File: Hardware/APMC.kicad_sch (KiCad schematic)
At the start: 180 parts, among them J1 Pin header Male 2x7 P:1.27, J10 Conn_01x03, J11 Conn_01x03, J12 Conn_01x08, J13 Conn_01x03, J14 Conn_01x04, J15 Pins 1x08, J2 USB4105-GF-A, J5 Terminal 1x5 P:3.5mm, J6 Terminal 1x5 P:3.5mm, J7 Terminal 1x5 P:3.5mm, J8 Conn_01x04, J9 Conn_01x04, M1 Logo_Open_Hardware_Small, Q1 FDT86102LZ, Q2 DMP6023LE, Q3 DMP6023LE, Q4 BSS123, Q5 DMP6023LE, Q6 DMP6023LE, Q7 BSS123, U10 TXU0202, U11 PCA9306, U12 LM74703/LM74704, U13 TPS62162DSG, U14 OPA2387DSG, U15 TPS259461A, U16 TUSB320, U17 LMR38015, U2 LCFE201202A, U3 TXU0202, U4 M95P32, U5 STM32U575CITx, U6 XTR200, U7 TPS7A2031PDBVR, U8 XTR200, U9 ADS1x2S14, X1 SiT8008Bx-7x, Y1 32.768kHz

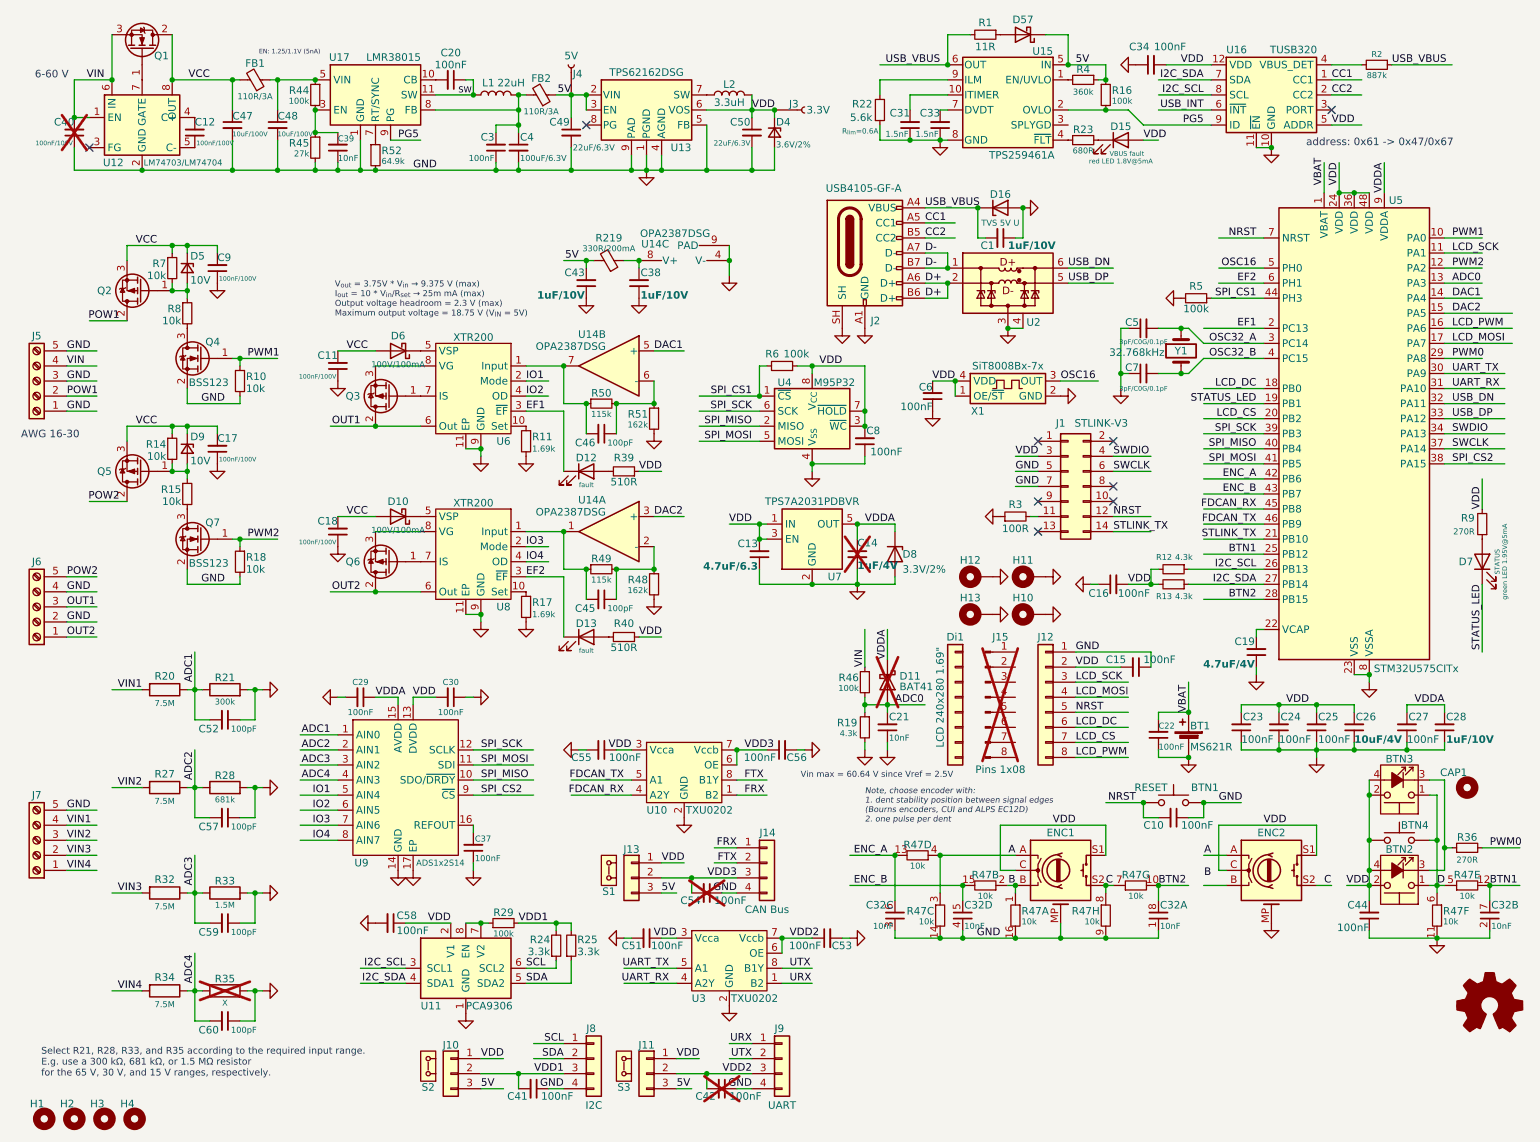
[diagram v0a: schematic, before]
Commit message: work on ADC communication
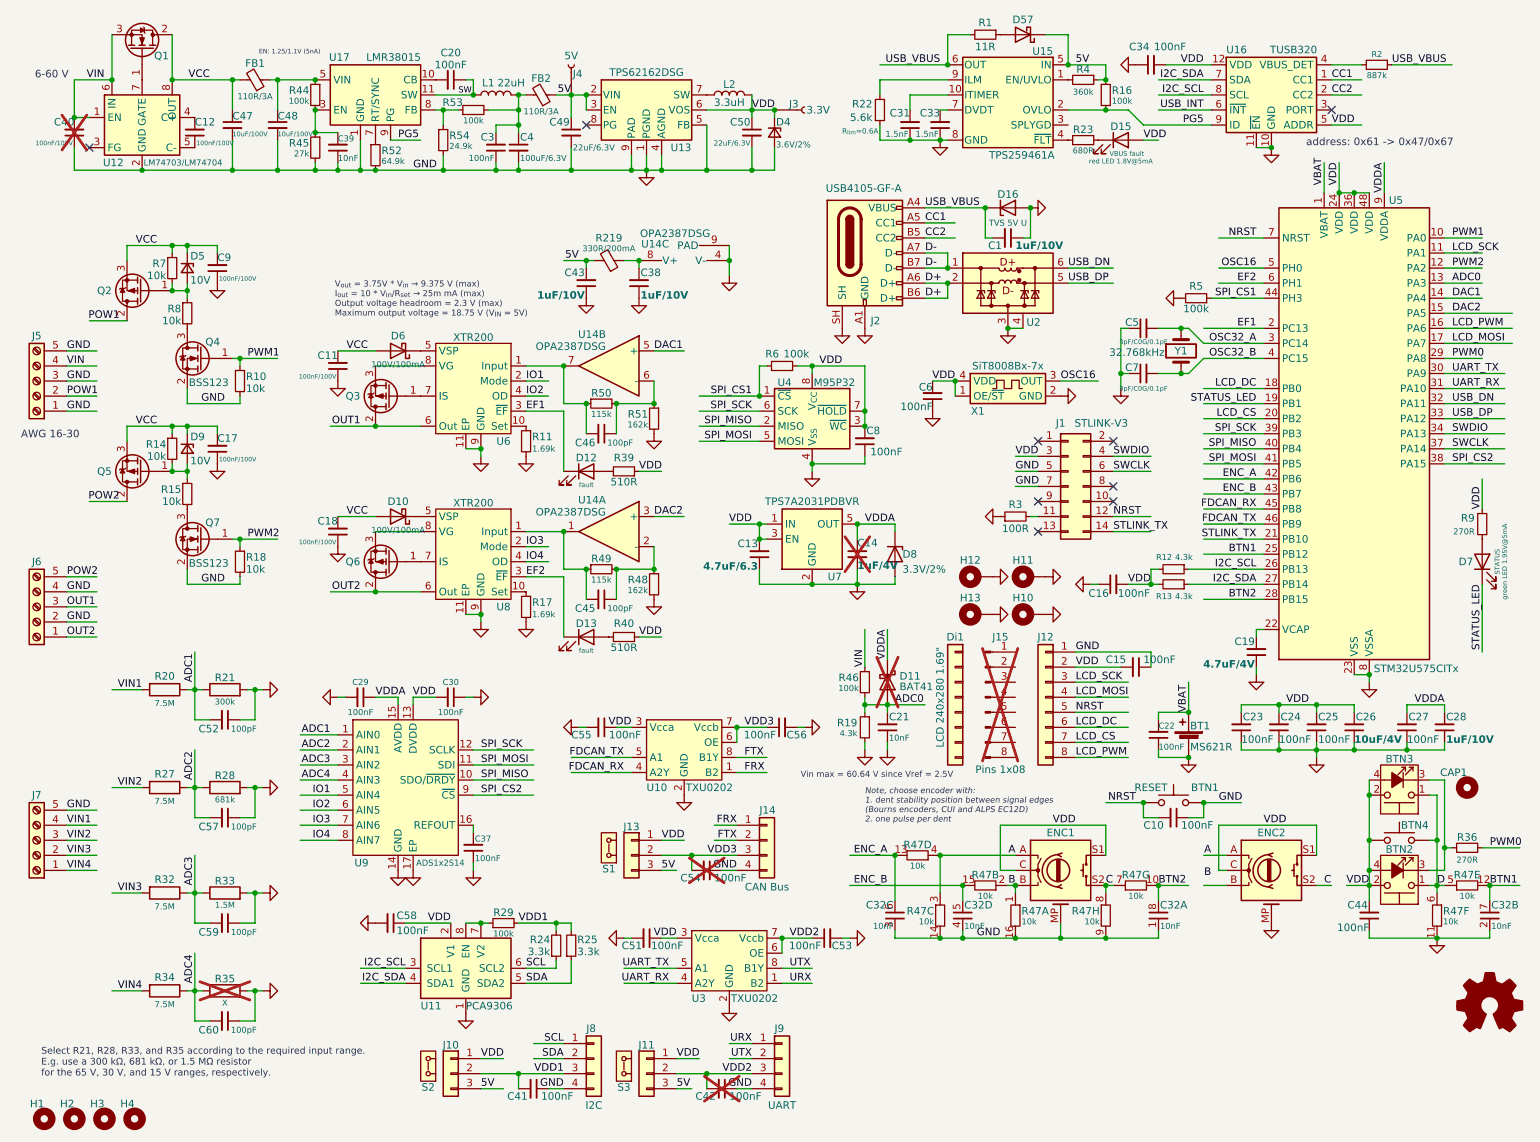
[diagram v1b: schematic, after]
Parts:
- added R53: 100k, Resistor_SMD:R_0603_1608Metric_Pad0.98x0.95mm_HandSolder, symbol Device:R_Small
- added R54: 24.9k, Resistor_SMD:R_0603_1608Metric_Pad0.98x0.95mm_HandSolder, symbol Device:R_Small
- BTN3: footprint tactile_switch_6x6_LED -> Custom:tactile_switch_6x6_LED
- D16: footprint Custom:D_SOD-123F -> Custom:D_SOD-123FL2; Alt many, eg. Littelfuse: SZSMF6L5.0AT3G, TSMC: SMF4L5.0A -> SMF4L5.0A, TPSMF4L5.0A, SMF4L5.0AT1G, PTVS5V0S1UTR,115; Mfg Littelfuse: SZSMF6L5.0AT3G -> Littelfuse: SMF4L5.0A; Mouser 576-SZSMF6L5.0AT3G -> 576-SMF4L5.0A
- L1: 10x10 DD1274AS-H-330M=P3, MSS1048-333MLC, CDRH104NP-330MC, 744771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 -> 1274AS-H-220M=P3, DD1274AS-H-220M=P3, MBH10145C-220MA=P3, B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; 8x8 (none) -> 1273AS-H-220M=P3, 1217AS-H-220M=P3; Ferrite 8x8 CDRH8D28NP-330NC, CDRH8D28NP-330NC, CDRH8D43HPNP-330NC, SCR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 -> (none); Mfg Murata: 1248AS-H-330M=P3 -> Murata: 1274AS-H-220M=P3; Mouser 81-1248AS-H-330MP3 -> 81-1274AS-H-220MP3; Murata 8x8 DEM8045Z-330M=P3, 1248AS-H-330M=P3 -> (none)
- U17: Alt (none) -> LMR38015SDRRR, LMR38015FDRRR, LMR38015SQDRRRQ1, LMR38025SQD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; Fixed5V LMR38015S5QDRRRQ1, LMR38015FS5QDRRRQ1, LMR38025S5QDRRRQ1 -> LMR38015S5QDRRRQ1, LMR38015FS5QDRRRQ1, LMR38025S5QDRRRQ1 (r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; Remarks (none) -> for LMR38025xxx (2.5A version) use inductor 33µH
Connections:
- net GND: now also R54.2
- net at C3.2, C4.1, FB2.2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: now also R53.2; no longer U17.8 (FB)
- new net: R53.1, R54.1, U17.8 (FB)
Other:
- moved on the sheet: C1, C54, C55, C56, D16, J13, J14, S1, U10

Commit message: ads1x2s14 gpio mgmt
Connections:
- net IO4 is gone; now on net IO3: U8.4 (OD), U9.8 (AIN7)
- net IO1: now also U6.4 (OD), U9.6 (AIN5); no longer U6.2 (Mode), U9.5 (AIN4)
- net IO2: now also U8.2 (Mode), U9.7 (AIN6); no longer U6.4 (OD), U9.6 (AIN5)
- net IO3: no longer U8.2 (Mode), U9.7 (AIN6)
- new net IO0: U6.2 (Mode), U9.5 (AIN4)
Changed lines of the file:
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@@
 		)
 	)
-	(label "IO1"
+	(label "IO0"
 		(at 64.77 144.78 180)
 		(effects
@@
 		)
 	)
-	(label "IO2"
+	(label "IO1"
 		(at 64.77 147.32 180)
 		(effects
@@
 		)
 	)
-	(label "IO4"
+	(label "IO3"
 		(at 64.77 152.4 180)
 		(effects
@@
 		)
 	)
-	(label "IO3"
+	(label "IO2"
 		(at 97.79 102.87 0)
 		(effects
@@
 		)
 	)
-	(label "IO3"
+	(label "IO2"
 		(at 64.77 149.86 180)
 		(effects
@@
 		)
 	)
-	(label "IO4"
+	(label "IO3"
 		(at 97.79 105.41 0)
 		(effects
@@
 		)
 	)
-	(label "IO1"
+	(label "IO0"
 		(at 97.79 74.93 0)
 		(effects
@@
 		)
 	)
-	(label "IO2"
+	(label "IO1"
 		(at 97.79 77.47 0)
 		(effects

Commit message: ads1x2s14 VMP impl
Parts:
- C40: now fitted; now in the parts list
